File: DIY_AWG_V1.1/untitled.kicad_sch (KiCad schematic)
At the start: 62 parts, among them U1 AMS1117-3.3, U2 ADP7118ARDZ-3.3-R7, U3 ADP7118ARDZ-3.3-R7, U4 TPS7A3301RGWR, U5 TPS7A4701RGWR, U6 TPS7A3301RGWR, U7 TPS7A4701RGWR

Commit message: Updated schematics
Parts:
- removed TP27: TestPoint, TestPoint:TestPoint_Pad_D2.0mm, symbol Connector:TestPoint
- added J1: Conn_01x04_Socket, Connector_JST:JST_XH_B4B-XH-A_1x04_P2.50mm_Vertical, symbol Connector:Conn_01x04_Socket
- added RF1, RF2, RF3, RF4, RF5: IPEX-01, easyeda2kicad:IPEX-SMD_3P-L2.6-W2.6-LS3.0_YUANDI_RF-001, symbol easyeda2kicad:IPEX-01
- added TP2, TP3: TestPoint, TestPoint:TestPoint_Pad_D2.0mm, symbol Connector:TestPoint
- TP10: renamed from TP8; footprint (none) -> TestPoint:TestPoint_Pad_D2.0mm
- TP6: renamed from TP4; footprint (none) -> TestPoint:TestPoint_Pad_D2.0mm
- TP7: renamed from TP5; footprint (none) -> TestPoint:TestPoint_Pad_D2.0mm
- TP8: renamed from TP6; footprint (none) -> TestPoint:TestPoint_Pad_D2.0mm
- TP9: renamed from TP7; footprint (none) -> TestPoint:TestPoint_Pad_D2.0mm
- renumbered TP2 to TP4, TP3 to TP5
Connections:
- net +10.0VA: now also RF2.1
- net +3.3VA_2: now also RF1.1
- net +5.0VA: now also RF4.1
- net +VSW12V0: now also J1.4 (Pin_4), TP2.1
- net -10.0VA: now also RF3.1
- net -5.0VA: now also RF5.1
- net GND: now also RF1.2, RF1.3, RF2.2, RF2.3, RF3.2, RF3.3, RF4.2, RF4.3, RF5.2, RF5.3, TP3.1
- net +5V renamed +VSW5V0
- net +VSW5V0: now also J1.1 (Pin_1)
- new net: J1.2 (Pin_2), J1.3 (Pin_3)
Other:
- moved on the sheet: C1, C10, C11, C12, C13, C14, C15, C16, C17, C18, C19, C2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

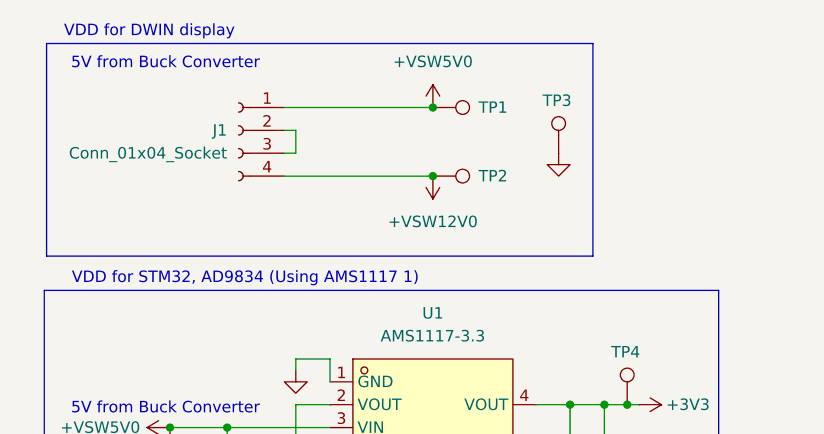
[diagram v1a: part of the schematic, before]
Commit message: Updated PCB design, uploaded necessary footprints and symbols for some components
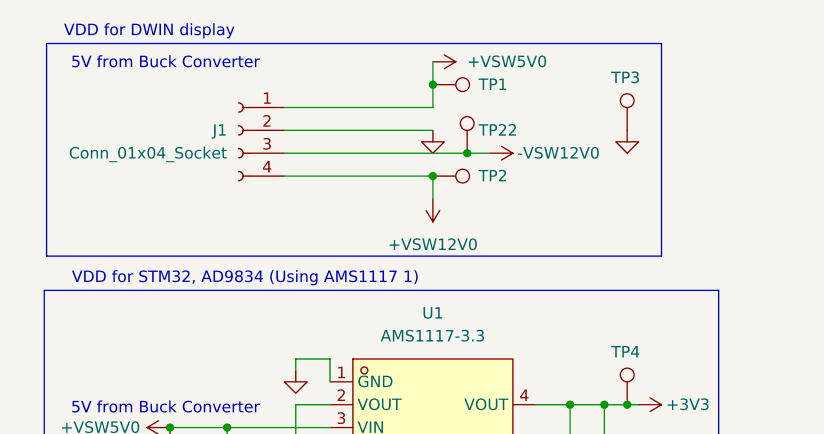
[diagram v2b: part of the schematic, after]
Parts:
- added TP22: TestPoint, TestPoint:TestPoint_Pad_D1.0mm, symbol Connector:TestPoint
- TP1, TP10, TP2, TP3, TP4, TP5, TP6, TP7, TP8, TP9: footprint TestPoint:TestPoint_Pad_D2.0mm -> TestPoint:TestPoint_Pad_D1.0mm
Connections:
- net -VSW12V0: now also J1.3 (Pin_3), TP22.1
- net GND: now also J1.2 (Pin_2)
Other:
- moved on the sheet: TP1, TP3

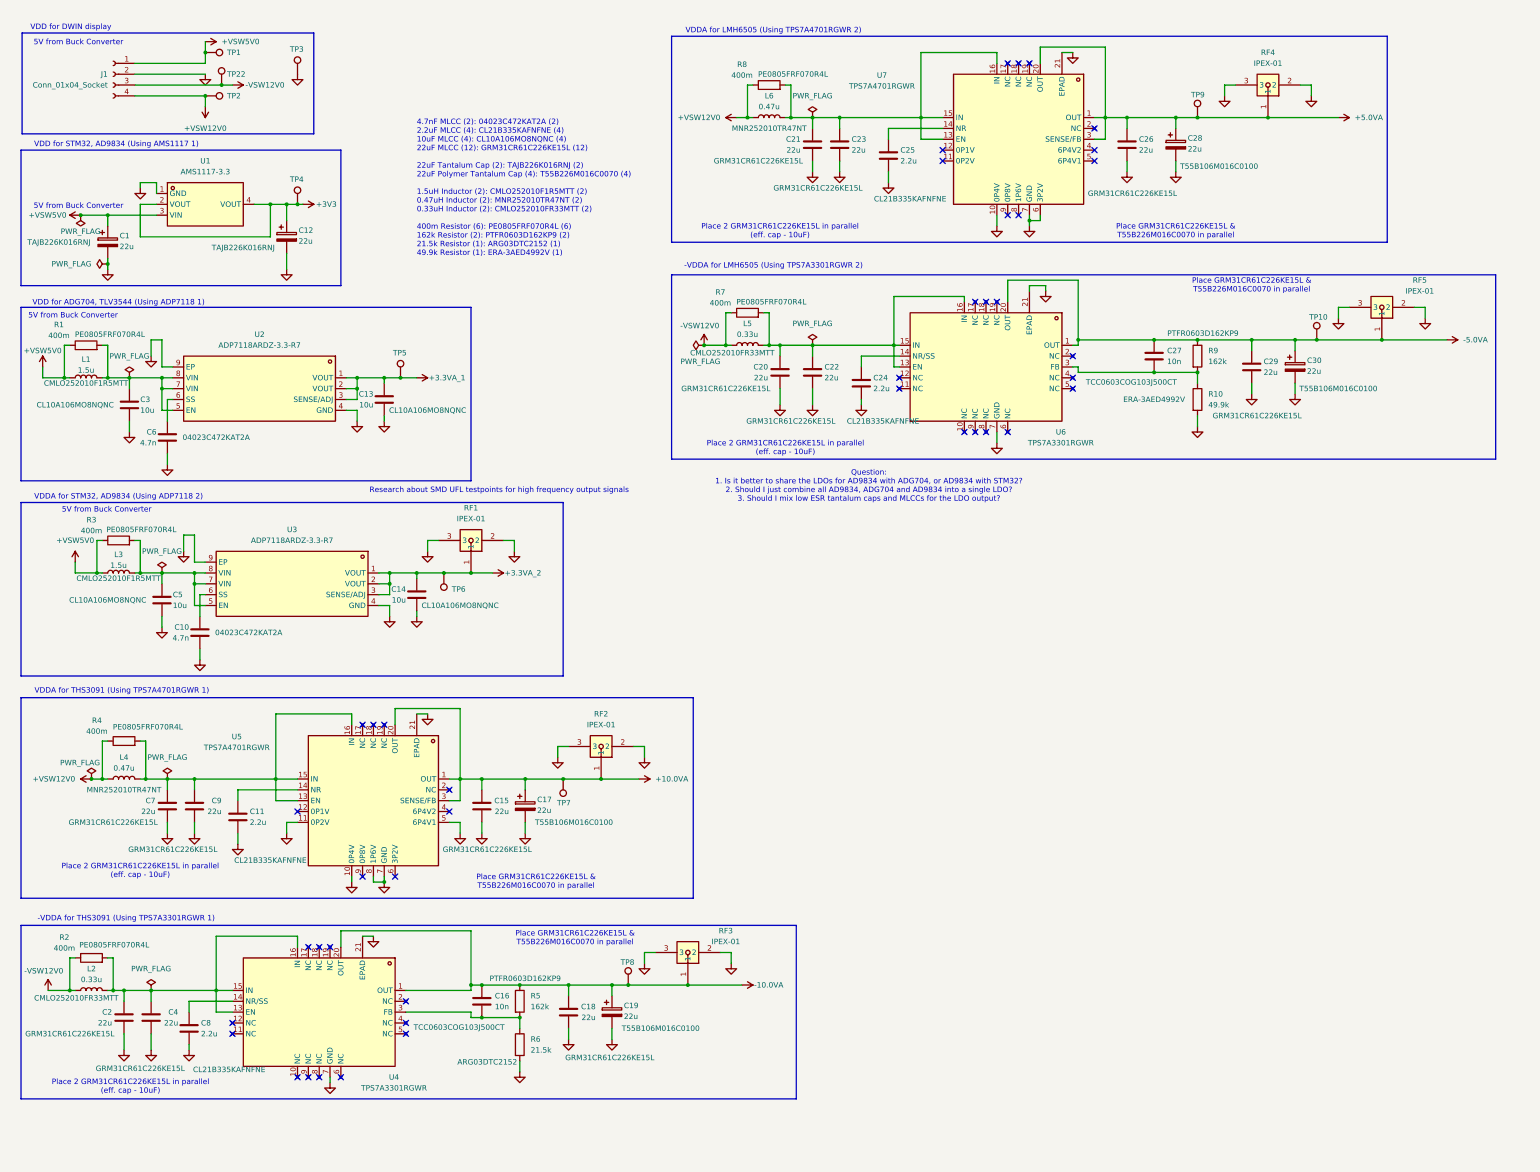
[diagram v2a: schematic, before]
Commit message: Edited the electrical schematics, PCB design
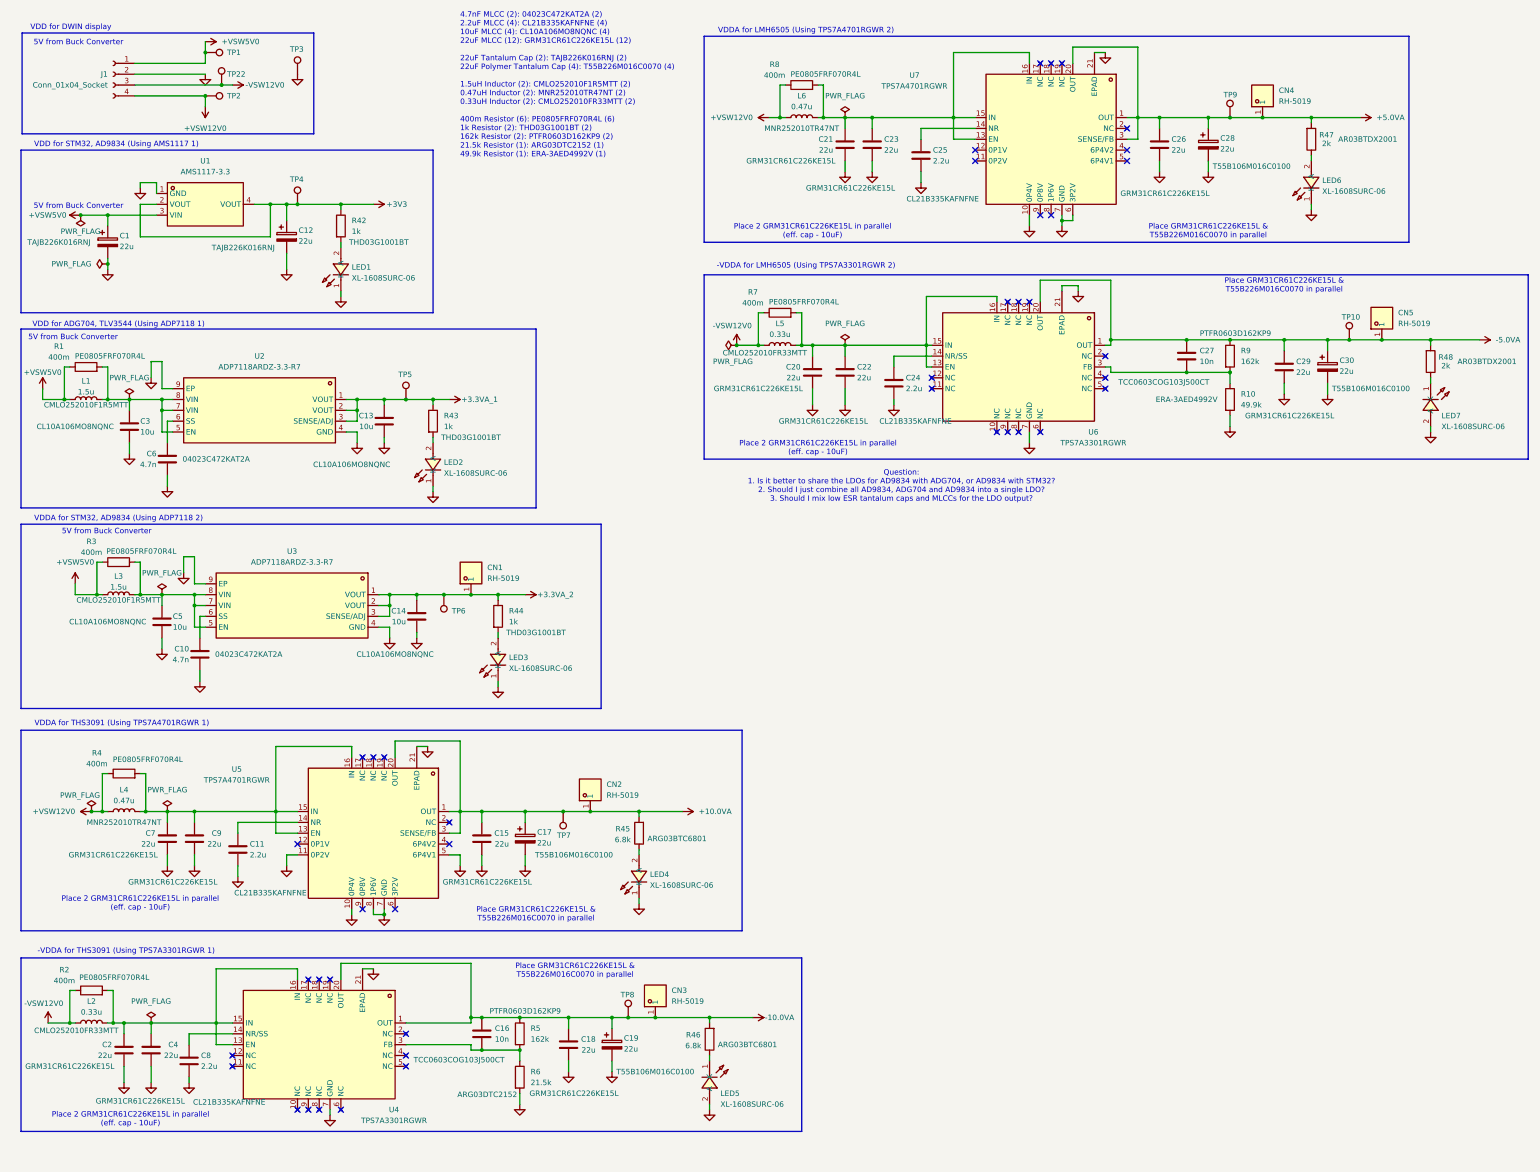
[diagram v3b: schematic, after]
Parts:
- removed RF1, RF2, RF3, RF4, RF5: IPEX-01, easyeda2kicad:IPEX-SMD_3P-L2.6-W2.6-LS3.0_YUANDI_RF-001, symbol easyeda2kicad:IPEX-01
- added CN1, CN2, CN3, CN4, CN5: RH-5019, easyeda2kicad:TESTPOINT-SMD_L3.8-W2.0_RH-5019, symbol easyeda2kicad:RH-5019
- added LED1, LED2, LED3, LED4, LED5, LED6, LED7: XL-1608SURC-06, easyeda2kicad:LED0603-RD_RED, symbol easyeda2kicad:XL-1608SURC-06
- added R42, R43, R44: 1k, Resistor_SMD:R_0603_1608Metric, symbol Device:R
- added R45, R46: 6.8k, Capacitor_SMD:C_0603_1608Metric, symbol Device:R
- added R47, R48: 2k, Resistor_SMD:R_0603_1608Metric, symbol Device:R
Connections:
- net +10.0VA: now also CN2.1, R45.2
- net +3.3VA_1: now also R43.1
- net +3.3VA_2: now also CN1.1, R44.1
- net +3V3: now also R42.1
- net +5.0VA: now also CN4.1, R47.2
- net -10.0VA: now also CN3.1, R46.2
- net -5.0VA: now also CN5.1, R48.2
- net GND: now also LED1.1 (K), LED2.1 (K), LED3.1 (K), LED4.1 (K), LED5.2 (A), LED6.1 (K), LED7.2 (A)
- new net: LED7.1 (K), R48.1
- new net: LED2.2 (A), R43.2
- new net: LED6.2 (A), R47.1
- new net: LED4.2 (A), R45.1
- new net: LED3.2 (A), R44.2
- new net: LED5.1 (K), R46.1
- new net: LED1.2 (A), R42.2
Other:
- note removed: "Research about SMD UFL testpoints for high frequency output signals"
- moved on the sheet: C10, C11, C13, C14, C15, C16, C17, C18, C19, C2, C20, C21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

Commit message: Updated schematic PCB design
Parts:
- added TP11, TP12, TP14, TP16, TP8: TestPoint, TestPoint:TestPoint_Pad_D1.0mm, symbol Connector:TestPoint
- renumbered R45 to R10, R46 to R11, R7 to R12, R8 to R13, R9 to R14, R10 to R15, R47 to R16, R48 to R17, R42 to R5, R43 to R6, R44 to R7, R5 to R8, R6 to R9, TP8 to TP10, TP9 to TP13, TP10 to TP15, TP22 to TP3, TP3 to TP4, TP4 to TP5, TP5 to TP6, TP6 to TP7, TP7 to TP9
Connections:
- net GND: now also TP11.1, TP12.1, TP14.1, TP16.1, TP8.1

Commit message: Updated PCB schematics
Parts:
- added LED10, LED8, LED9: XL-1608SURC-06, easyeda2kicad:LED0603-RD_RED, symbol easyeda2kicad:XL-1608SURC-06
- added R51: 1k, Resistor_SMD:R_0603_1608Metric, symbol Device:R
- added R52, R53: 2k, Resistor_SMD:R_0603_1608Metric, symbol Device:R
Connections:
- net +VSW12V0: now also R53.2
- net +VSW5V0: now also R51.1
- net -VSW12V0: now also R52.2
- net GND: now also LED10.1 (K), LED8.1 (K), LED9.2 (A)
- new net: LED9.1 (K), R52.1
- new net: LED8.2 (A), R51.2
- new net: LED10.2 (A), R53.1
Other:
- moved on the sheet: C1, C10, C11, C12, C13, C14, C15, C16, C17, C18, C19, C2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
